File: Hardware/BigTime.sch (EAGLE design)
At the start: 19 parts, among them U2 ATMEGA328P_TQFP, Y1 32.768kHz

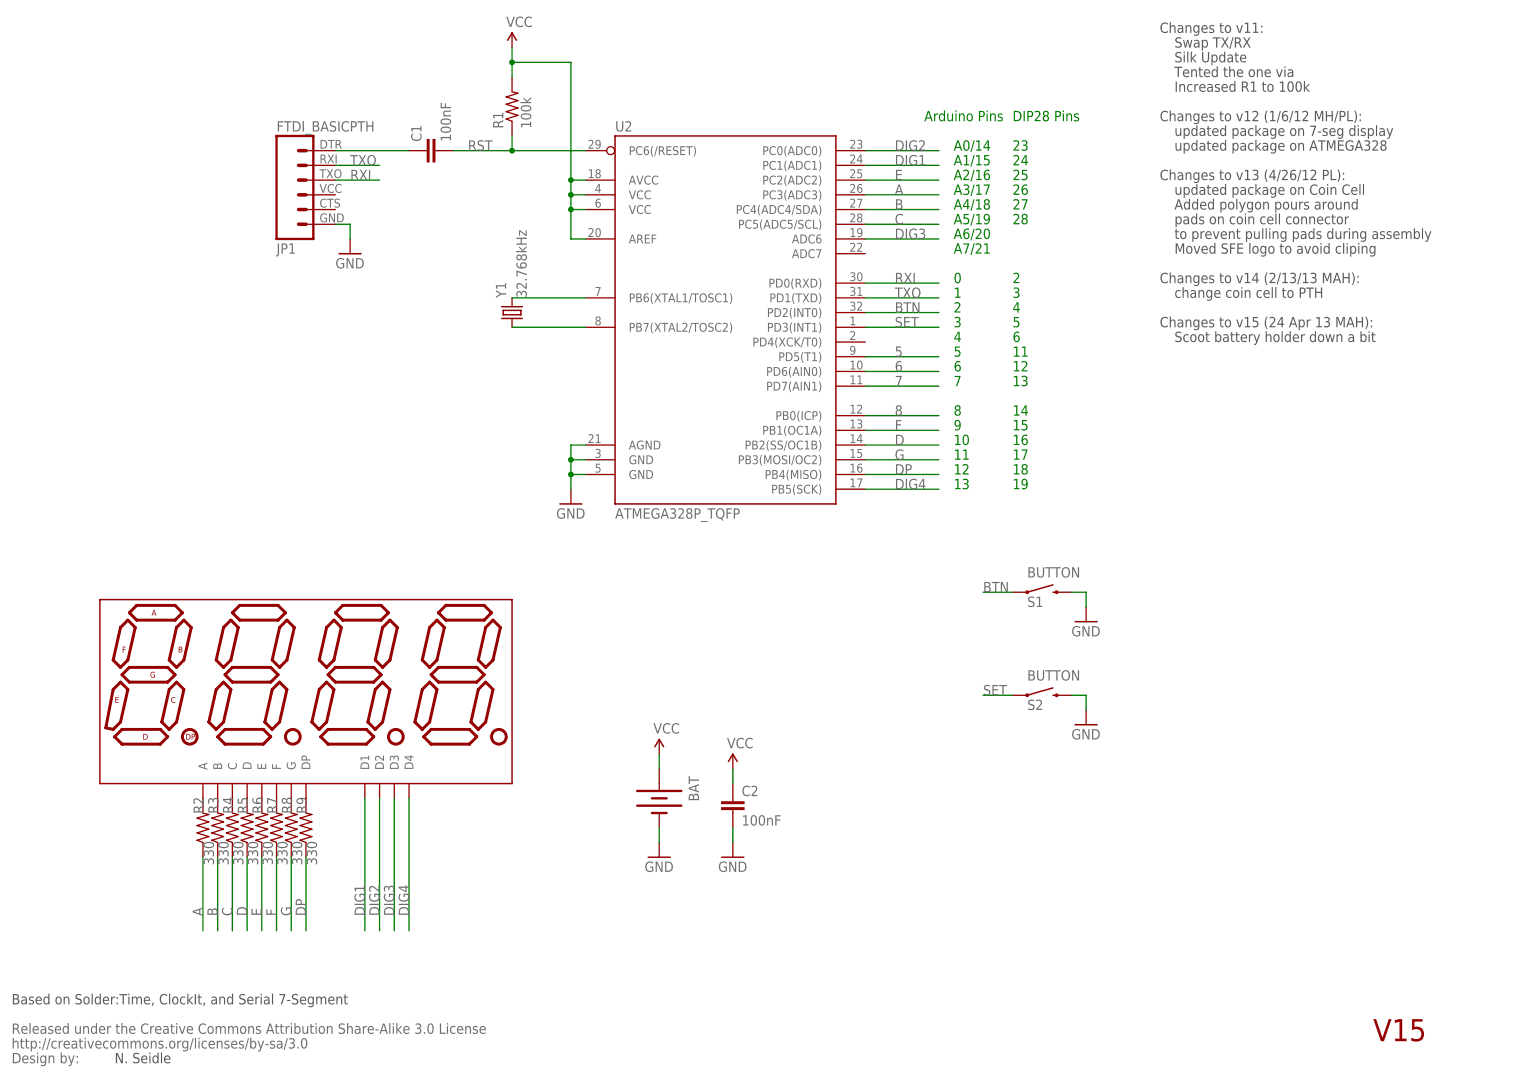
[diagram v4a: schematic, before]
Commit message: fit 1" footprint
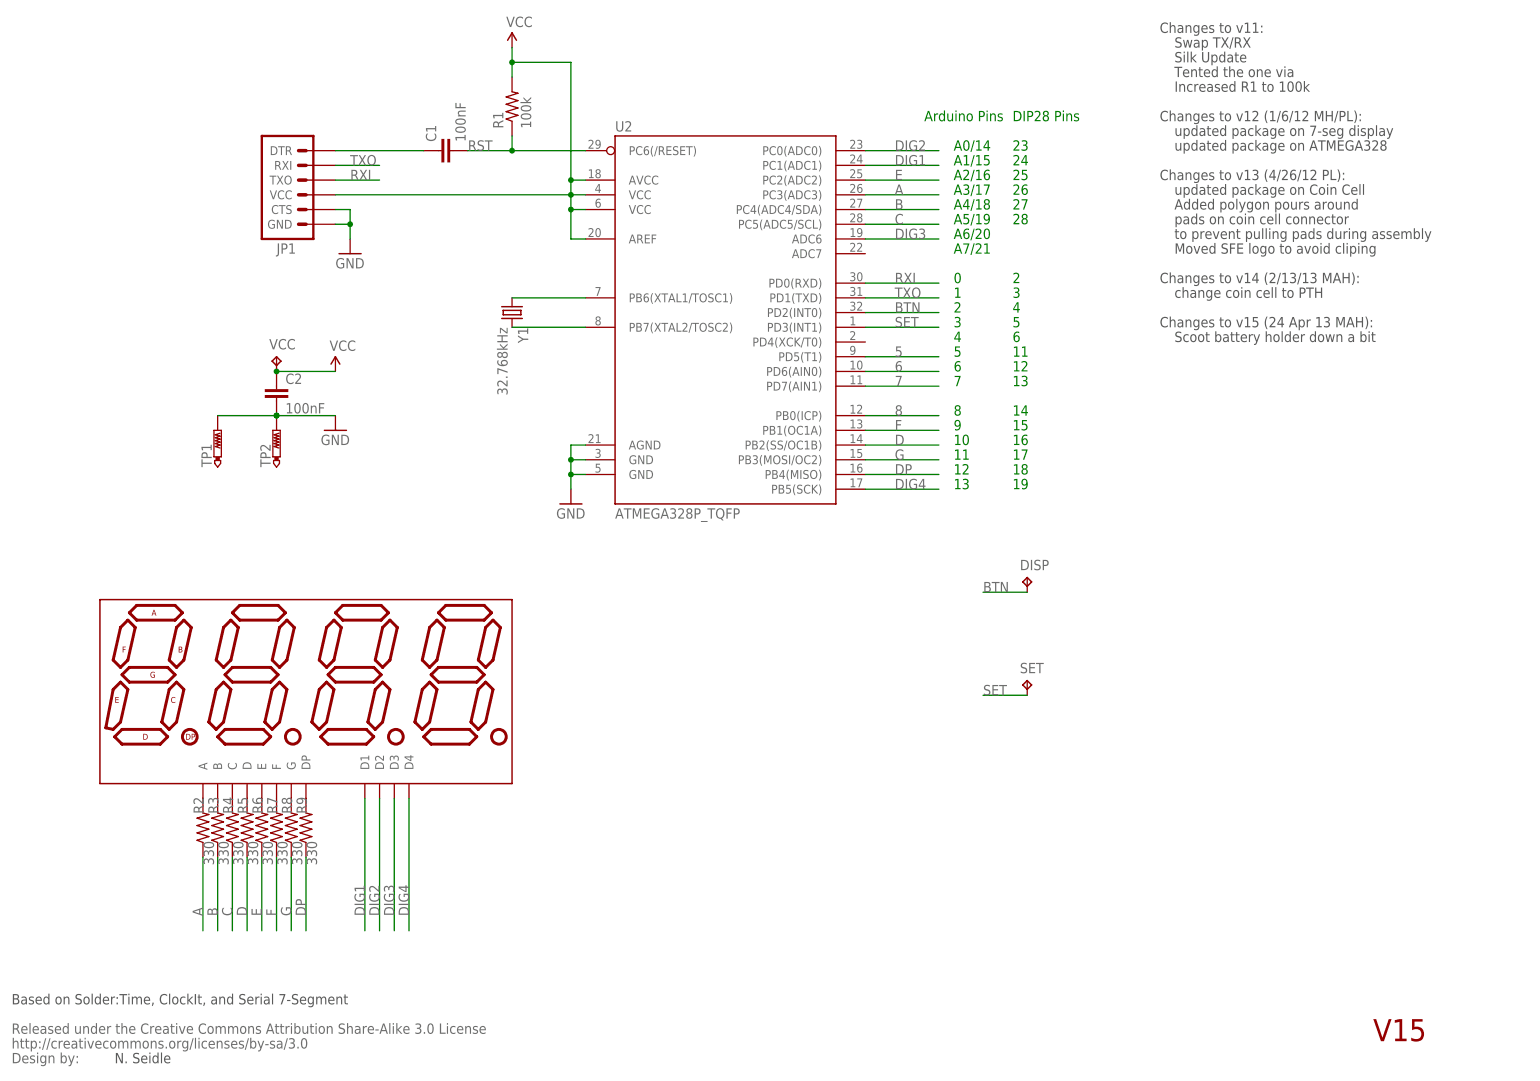
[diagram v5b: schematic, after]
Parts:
- removed BAT: (no value), SparkFun-Electromechanical:BATTERYFOB
- removed S1, S2: BUTTON, SparkFun-Electromechanical:SWITCH-MOMENTARY-2SIDE_EZ
- added DISP, SET: TPPAD1-13, testpad:TPPAD1-13
- added TP1, TP2: PTR1PAD1-13, testpad:PTR1PAD1-13
- added VCC: TPTP20R, testpad:TPTP20R
- C1, C2: device SparkFun-Passives:CAP0402-CAP -> resistor:C-EUC0201
- JP1: value FTDI_BASICPTH -> (none); device SparkFun:FTDI_BASICPTH -> SparkFun-Connectors:ARDUINO_SERIAL_PROGRAMSMD
- R1, R2, R3, R4, R5, R6, R7, R8, R9: device SparkFun-Passives:RESISTOR0402-RES -> resistor:R-US_R0201
- Y1: device SparkFun-FreqCtrl:CRYSTAL32-SMD -> crystal:CRYSTALTC26H
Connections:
- net BTN: now also DISP.TP; no longer S1.1
- net GND: now also JP1.CTS, JP1.GND, TP1.TP, TP2.TP; no longer BAT.-, JP1.6, S1.2, S2.2
- net N$1: now also Y1.2; no longer Y1.1
- net N$2: now also Y1.1; no longer Y1.2
- net N$3: now also JP1.DTR; no longer JP1.1
- net RXI: now also JP1.TXO; no longer JP1.3
- net SET: now also SET.TP; no longer S2.1
- net TXO: now also JP1.RXI; no longer JP1.2
- net VCC: now also JP1.VCC, VCC.TP; no longer BAT.+
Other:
- moved on the sheet: C1, C2, JP1, Y1

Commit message: fit
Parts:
- removed DISP, SET: TPPAD1-13, testpad:TPPAD1-13
- removed TP1, TP2: PTR1PAD1-13, testpad:PTR1PAD1-13
- removed U$2: CREATIVE_COMMONS, SparkFun:CREATIVE_COMMONS
- added TP3, TP4: (no value), SparkFun-Connectors:M01PTH
- added TP5, TP6: (no value), adafruit:PINHD-1X1CB
- DISP1: device SparkFun-Displays:7-SEGMENT-4DIGIT-COUNTER-HP-BUBBLE-SM -> BigTime:7-SEGMENT-4DIGIT-COUNTER-HP-BUBBLE-SM
- JP1: value (none) -> FTDI_DEVICERA_SMT; device SparkFun-Connectors:ARDUINO_SERIAL_PROGRAMSMD -> BigTime:FTDI_DEVICERA_SMT
- Y1: device crystal:CRYSTALTC26H -> BigTime:CRYSTALTC26H
- renumbered VCC to BAT+
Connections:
- net A: now also U2.PC5(ADC5/SCL); no longer U2.PC3(ADC3)
- net B: now also U2.PC3(ADC3); no longer U2.PC4(ADC4/SDA)
- net BTN: now also TP3.1; no longer DISP.TP
- net C: now also U2.PC2(ADC2); no longer U2.PC5(ADC5/SCL)
- net D: now also U2.PB3(MOSI/OC2); no longer U2.PB2(SS/OC1B)
- net DIG1: now also U2.PC4(ADC4/SDA); no longer U2.PC1(ADC1)
- net DIG4: now also U2.PB2(SS/OC1B); no longer U2.PB5(SCK)
- net DP: now also U2.PB5(SCK); no longer U2.PB4(MISO)
- net E: now also U2.PC1(ADC1); no longer U2.PC2(ADC2)
- net F: now also U2.PB4(MISO); no longer U2.PB1(OC1A)
- net G: now also U2.PB1(OC1A); no longer U2.PB3(MOSI/OC2)
- net GND: now also TP5.1, TP6.1; no longer TP1.TP, TP2.TP
- net SET: now also TP4.1; no longer SET.TP
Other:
- note removed: "Added polygon pours around"
- note removed: "Based on Solder:Time, ClockIt, and Serial 7-Segment"
- note removed: "Changes to v11:"
- note removed: "Changes to v12 (1/6/12 MH/PL):"
- note removed: "Changes to v13 (4/26/12 PL):"
- note removed: "Changes to v14 (2/13/13 MAH):"
- note removed: "Changes to v15 (24 Apr 13 MAH):"
- note removed: "Increased R1 to 100k"
- note removed: "Moved SFE logo to avoid cliping"
- note removed: "N. Seidle"
- note removed: "Scoot battery holder down a bit"
- note removed: "Silk Update"
- note removed: "Swap TX/RX"
- note removed: "Tented the one via"
- note removed: "V15"
- note removed: "change coin cell to PTH"
- note removed: "pads on coin cell connector"
- note removed: "to prevent pulling pads during assembly"
- note removed: "updated package on 7-seg display"
- note removed: "updated package on ATMEGA328"
- note removed: "updated package on Coin Cell"

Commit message: bigger components, no pullup on reset
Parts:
- removed R1: 100k, resistor:R-US_R0201
- C1, C2: device resistor:C-EUC0201 -> resistor:C-EUC0402
- R2, R3, R4, R5, R6, R7, R8, R9: device resistor:R-US_R0201 -> resistor:R-US_R0402
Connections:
- net D: now also U2.PB2(SS/OC1B); no longer U2.PB3(MOSI/OC2)
- net DIG4: now also U2.PB3(MOSI/OC2); no longer U2.PB2(SS/OC1B)
- net RST: no longer R1.1
- net VCC: no longer R1.2

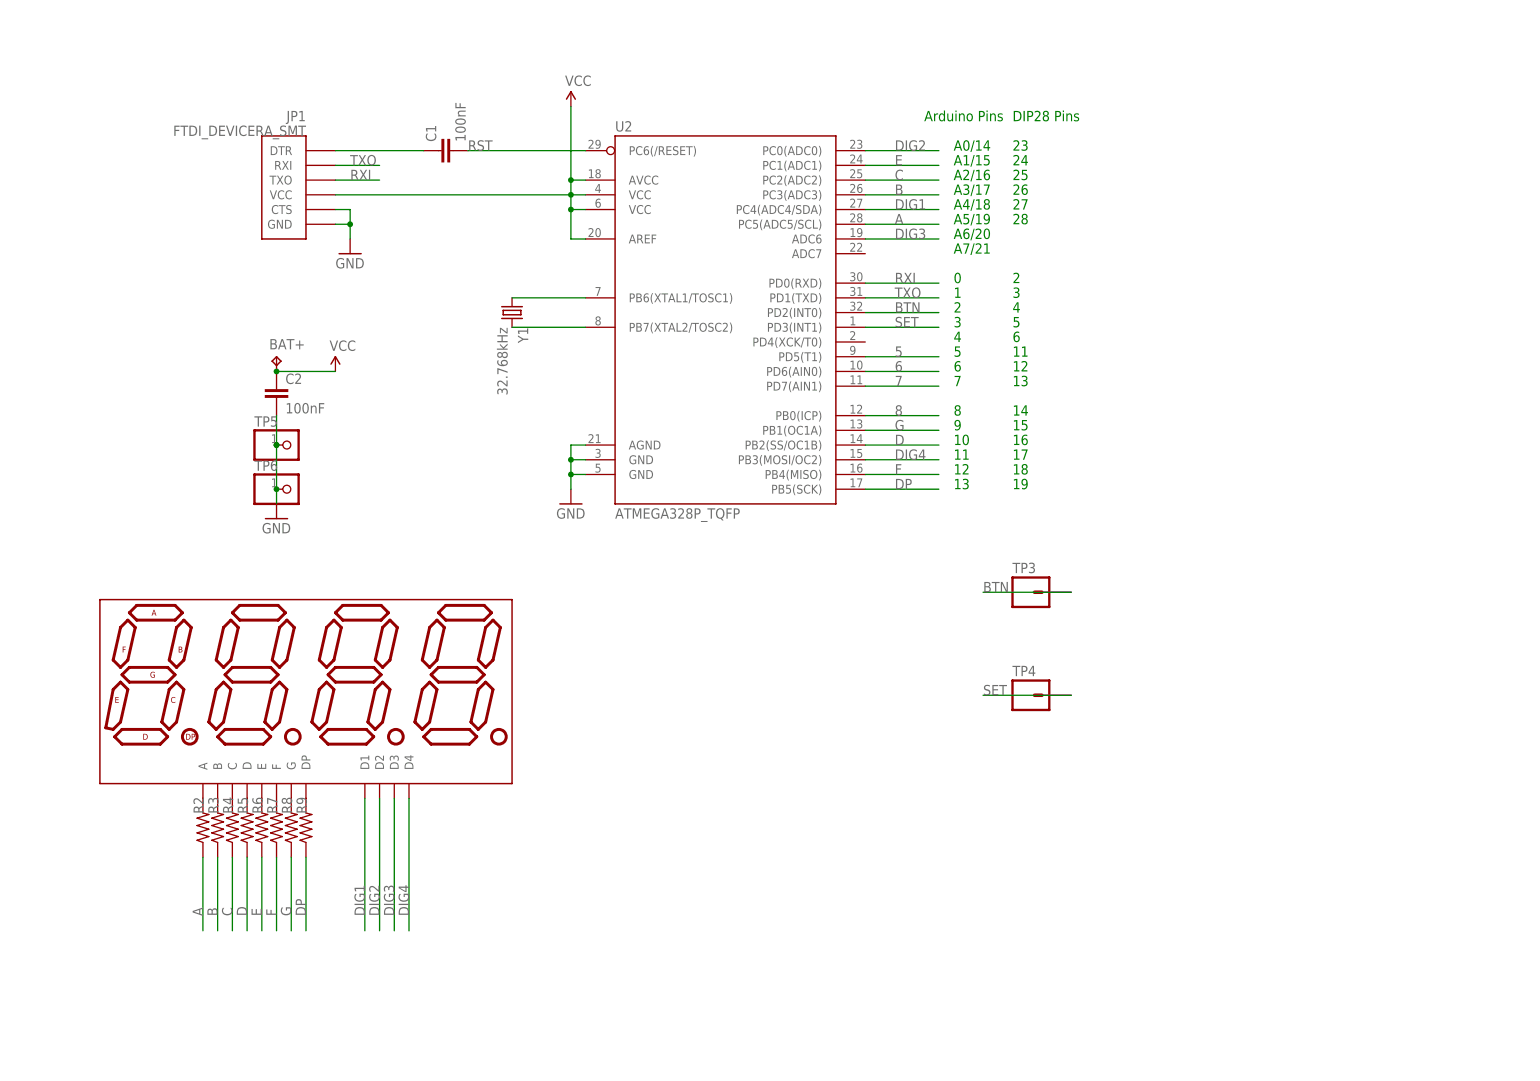
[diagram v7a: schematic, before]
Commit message: rename back to BigTime
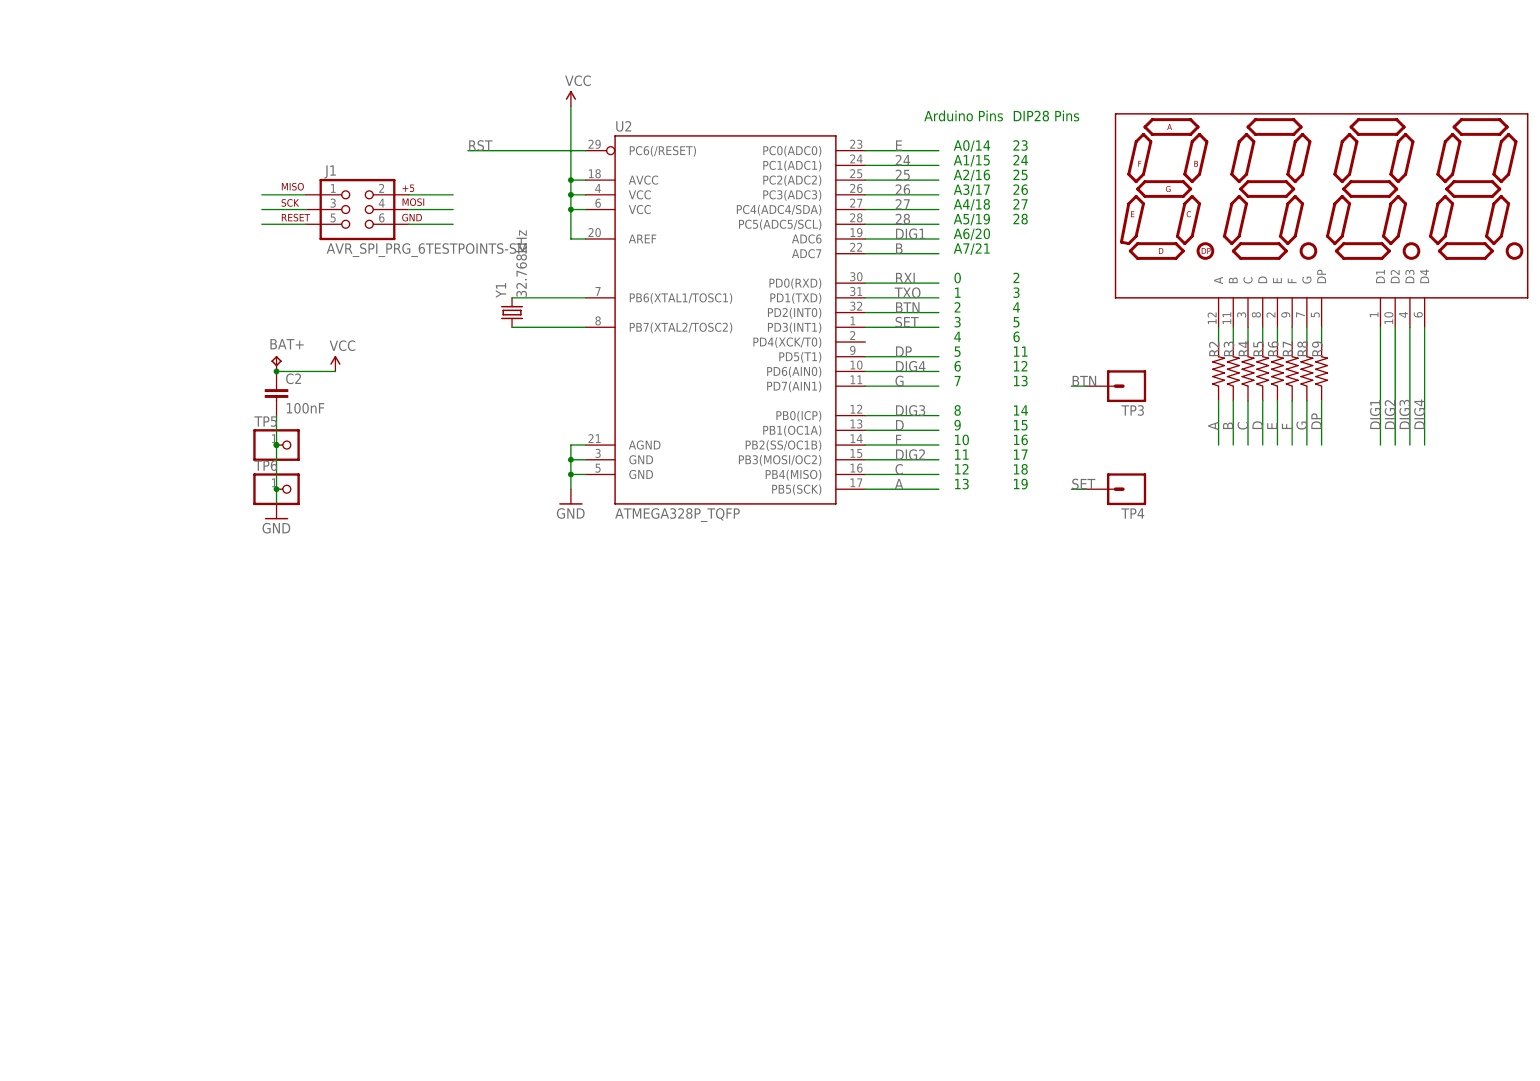
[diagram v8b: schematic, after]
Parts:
- removed C1: 100nF, resistor:C-EUC0402
- removed JP1: FTDI_DEVICERA_SMT, BigTime:FTDI_DEVICERA_SMT
- added J1: AVR_SPI_PRG_6TESTPOINTS-SM, Connectors:AVR_SPI_PRG_6TESTPOINTS-SM
- C2: device resistor:C-EUC0402 -> resistor:C-EUC0805
- R2, R3, R4, R5, R6, R7, R8, R9: device resistor:R-US_R0402 -> resistor:R-US_R0805
- TP3, TP4: device SparkFun-Connectors:M01PTH -> Connectors:M01EDGE_CONTACT
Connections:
- removed net 5: U2.PD5(T1)
- removed net 6: U2.PD6(AIN0)
- removed net 7: U2.PD7(AIN1)
- removed net 8: U2.PB0(ICP)
- removed net N$3: C1.1, JP1.DTR
- new net 24: U2.PC1(ADC1)
- new net 25: U2.PC2(ADC2)
- new net 26: U2.PC3(ADC3)
- new net 27: U2.PC4(ADC4/SDA)
- new net 28: U2.PC5(ADC5/SCL)
- net A: now also J1.3, U2.PB5(SCK); no longer U2.PC5(ADC5/SCL)
- net B: now also U2.ADC7; no longer U2.PC3(ADC3)
- net C: now also J1.1, U2.PB4(MISO); no longer U2.PC2(ADC2)
- net D: now also U2.PB1(OC1A); no longer U2.PB2(SS/OC1B)
- net DIG1: now also U2.ADC6; no longer U2.PC4(ADC4/SDA)
- net DIG2: now also J1.4, U2.PB3(MOSI/OC2); no longer U2.PC0(ADC0)
- net DIG3: now also U2.PB0(ICP); no longer U2.ADC6
- net DIG4: now also U2.PD6(AIN0); no longer U2.PB3(MOSI/OC2)
- net DP: now also U2.PD5(T1); no longer U2.PB5(SCK)
- net E: now also U2.PC0(ADC0); no longer U2.PC1(ADC1)
- net F: now also U2.PB2(SS/OC1B); no longer U2.PB4(MISO)
- net G: now also U2.PD7(AIN1); no longer U2.PB1(OC1A)
- net GND: now also J1.6; no longer JP1.CTS, JP1.GND
- net N$1: now also Y1.1; no longer Y1.2
- net N$2: now also Y1.2; no longer Y1.1
- net RST: now also J1.5; no longer C1.2
- net RXI: no longer JP1.TXO
- net TXO: no longer JP1.RXI
- net VCC: now also J1.2; no longer JP1.VCC
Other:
- moved on the sheet: R2, R3, R4, R5, R6, R7, R8, R9, TP3, TP4, Y1
